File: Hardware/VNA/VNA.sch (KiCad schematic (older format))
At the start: 12 parts, among them J1 USB_B_Micro, J2 USB_A, J3 SMA, J4 SMA

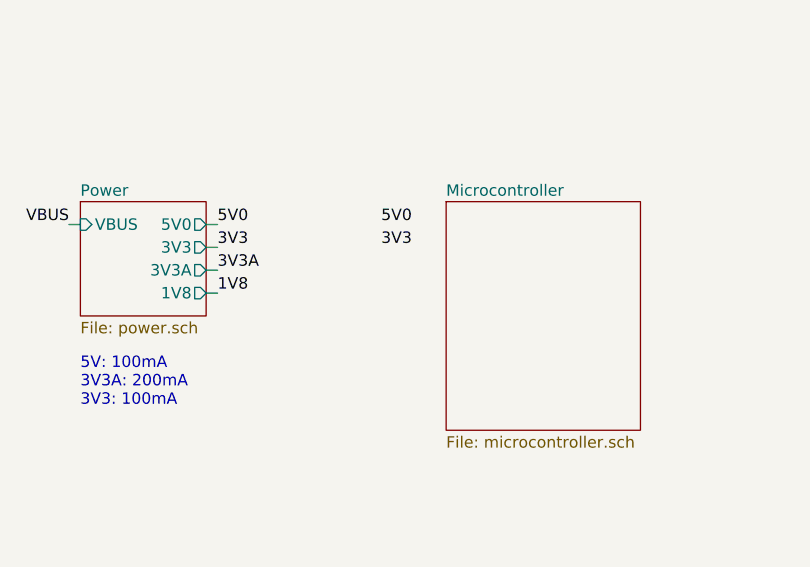
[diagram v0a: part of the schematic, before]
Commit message: added footprints and 3d models
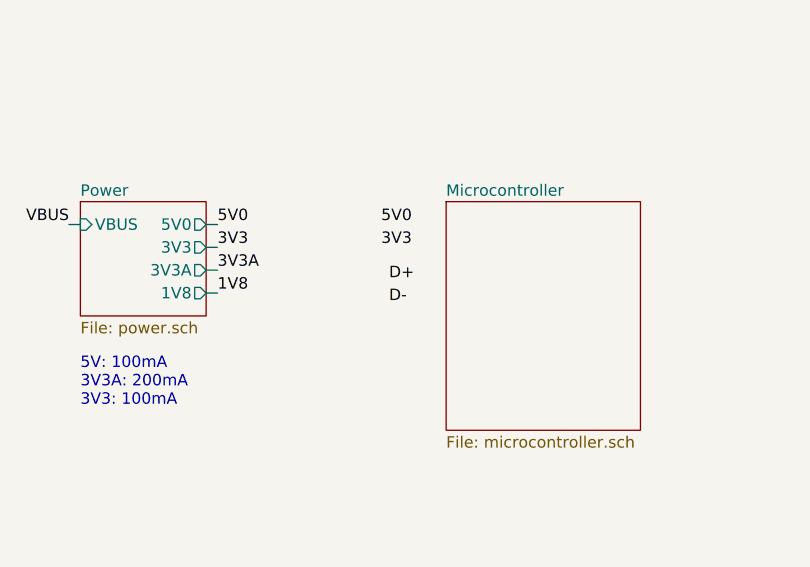
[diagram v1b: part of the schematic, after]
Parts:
- C1, C2, C3, C4: footprint (none) -> Capacitor_SMD:C_0402_1005Metric
- J1: footprint (none) -> VNA_Footprints:MicroUSB_Aliexpress
- J2: footprint (none) -> VNA_Footprints:676432911_usbA
- J3, J4: footprint (none) -> VNA_Footprints:SMA_EDGE_MOUNT
- R1, R2, R3, R4: footprint (none) -> Resistor_SMD:R_0402_1005Metric
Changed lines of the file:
@@
 F 0 "C3" V 5450 1550 50  0000 C CNN
 F 1 "1n" V 5750 1550 50  0000 C CNN
-F 2 "" H 5638 1400 50  0001 C CNN
+F 2 "Capacitor_SMD:C_0402_1005Metric" H 5638 1400 50  0001 C CNN
 F 3 "~" H 5600 1550 50  0001 C CNN
 	1    5600 1550
@@
 F 0 "C2" V 3250 1550 50  0000 C CNN
 F 1 "1n" V 3550 1550 50  0000 C CNN
-F 2 "" H 3438 1400 50  0001 C CNN
+F 2 "Capacitor_SMD:C_0402_1005Metric" H 3438 1400 50  0001 C CNN
 F 3 "~" H 3400 1550 50  0001 C CNN
 	1    3400 1550
@@
 F 0 "C1" V 2800 1800 50  0000 C CNN
 F 1 "1n" V 3100 1800 50  0000 C CNN
-F 2 "" H 2988 1650 50  0001 C CNN
+F 2 "Capacitor_SMD:C_0402_1005Metric" H 2988 1650 50  0001 C CNN
 F 3 "~" H 2950 1800 50  0001 C CNN
 	1    2950 1800
@@
 F 0 "R1" H 3370 2096 50  0000 L CNN
 F 1 "49R9" H 3370 2005 50  0000 L CNN
-F 2 "" V 3230 2050 50  0001 C CNN
+F 2 "Resistor_SMD:R_0402_1005Metric" V 3230 2050 50  0001 C CNN
 F 3 "~" H 3300 2050 50  0001 C CNN
 	1    3300 2050
@@
 F 0 "C4" V 7350 1550 50  0000 C CNN
 F 1 "1n" V 7650 1550 50  0000 C CNN
-F 2 "" H 7538 1400 50  0001 C CNN
+F 2 "Capacitor_SMD:C_0402_1005Metric" H 7538 1400 50  0001 C CNN
 F 3 "~" H 7500 1550 50  0001 C CNN
 	1    7500 1550
@@
 F 0 "J1" H 800 7450 50  0000 C CNN
 F 1 "USB_B_Micro" H 900 7350 50  0000 C CNN
-F 2 "" H 1100 6950 50  0001 C CNN
+F 2 "VNA_Footprints:MicroUSB_Aliexpress" H 1100 6950 50  0001 C CNN
 F 3 "~" H 1100 6950 50  0001 C CNN
 	1    950  7000
@@
 F 0 "J4" H 10100 1525 50  0000 L CNN
 F 1 "SMA" H 9850 1700 50  0000 L CNN
-F 2 "" H 10000 1550 50  0001 C CNN
+F 2 "VNA_Footprints:SMA_EDGE_MOUNT" H 10000 1550 50  0001 C CNN
 F 3 " ~" H 10000 1550 50  0001 C CNN
 	1    10000 1550
@@
 F 0 "R3" H 9370 2296 50  0000 L CNN
 F 1 "16R6" H 9370 2205 50  0000 L CNN
-F 2 "" V 9230 2250 50  0001 C CNN
+F 2 "Resistor_SMD:R_0402_1005Metric" V 9230 2250 50  0001 C CNN
 F 3 "~" H 9300 2250 50  0001 C CNN
 	1    9300 2250
@@
 F 0 "R2" V 9000 2500 50  0000 C CNN
 F 1 "16R6" V 9200 2500 50  0000 C CNN
-F 2 "" V 9030 2500 50  0001 C CNN
+F 2 "Resistor_SMD:R_0402_1005Metric" V 9030 2500 50  0001 C CNN
 F 3 "~" H 9100 2500 50  0001 C CNN
 	1    9100 2500
@@
 F 0 "R4" V 9400 2500 50  0000 C CNN
 F 1 "16R6" V 9600 2500 50  0000 C CNN
-F 2 "" V 9430 2500 50  0001 C CNN
+F 2 "Resistor_SMD:R_0402_1005Metric" V 9430 2500 50  0001 C CNN
 F 3 "~" H 9500 2500 50  0001 C CNN
 	1    9500 2500
@@
 F 0 "J3" H 10050 4475 50  0000 L CNN
 F 1 "SMA" H 9800 4650 50  0000 L CNN
-F 2 "" H 9950 4500 50  0001 C CNN
+F 2 "VNA_Footprints:SMA_EDGE_MOUNT" H 9950 4500 50  0001 C CNN
 F 3 " ~" H 9950 4500 50  0001 C CNN
 	1    9950 4500
@@
 F 0 "J2" H 1850 7450 50  0000 C CNN
 F 1 "USB_A" H 1900 7350 50  0000 C CNN
-F 2 "" H 2150 6950 50  0001 C CNN
+F 2 "VNA_Footprints:676432911_usbA" H 2150 6950 50  0001 C CNN
 F 3 " ~" H 2150 6950 50  0001 C CNN
 	1    2000 7000
@@
 Text Label 6150 2350 2    50   ~ 0
 PA_PWRDN
+Text Label 3000 4550 0    50   ~ 0
+D+
+Text Label 3000 4650 0    50   ~ 0
+D-
 $EndSCHEMATC

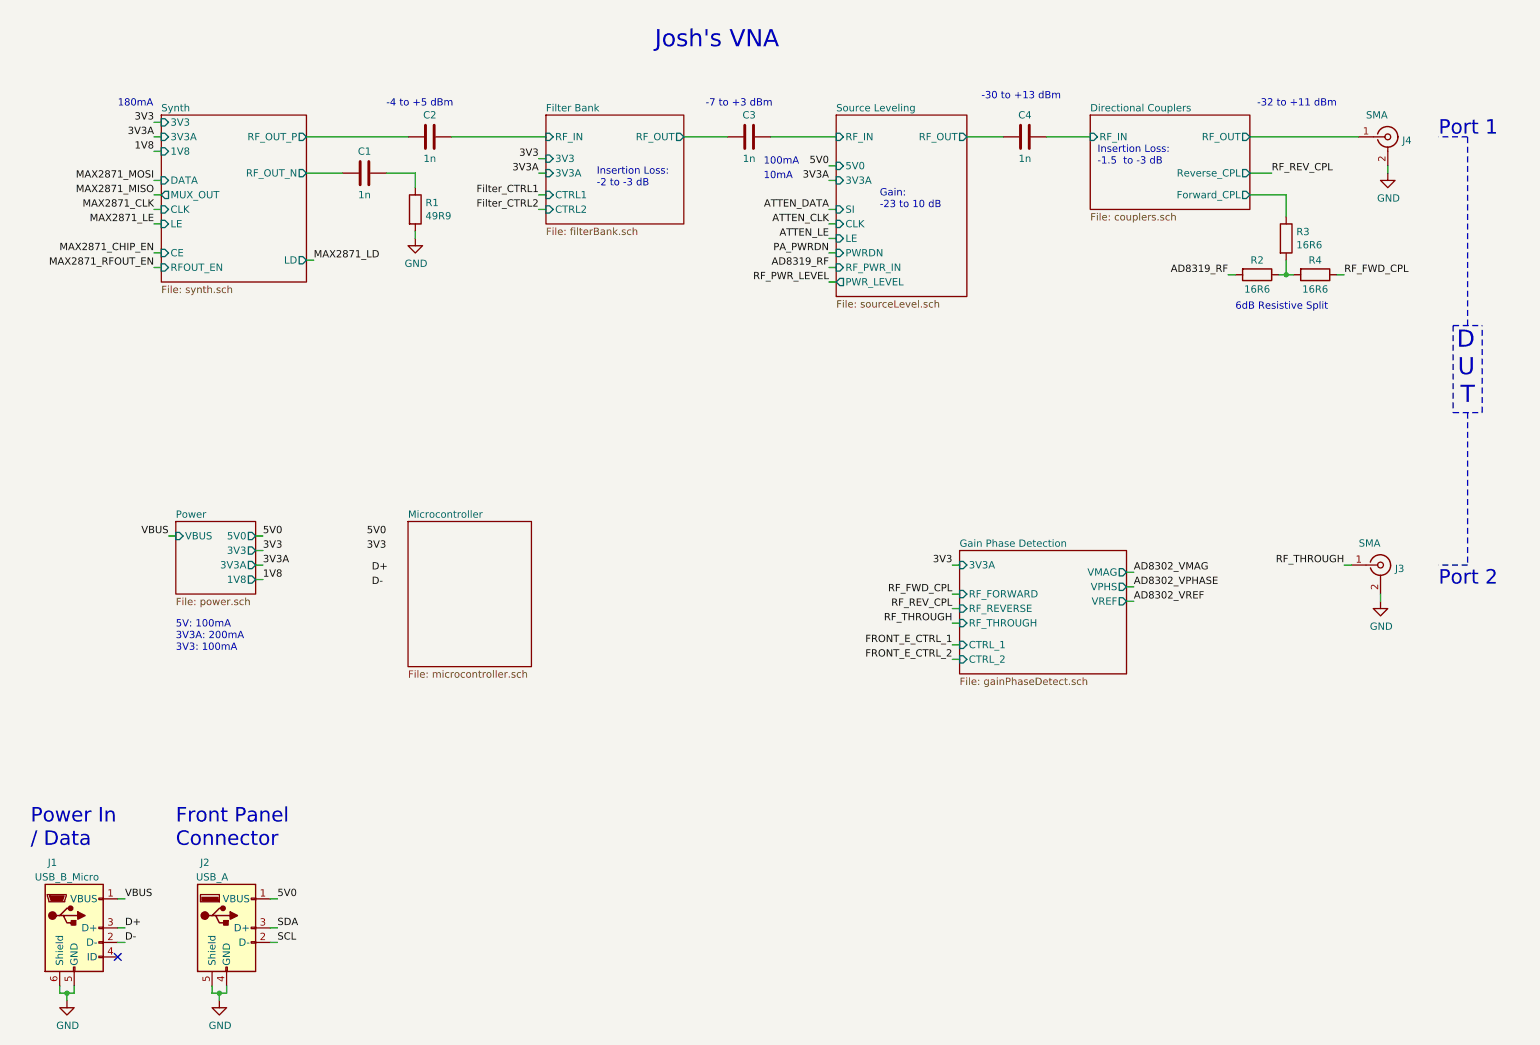
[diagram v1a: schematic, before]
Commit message: prelim schematic capture complete
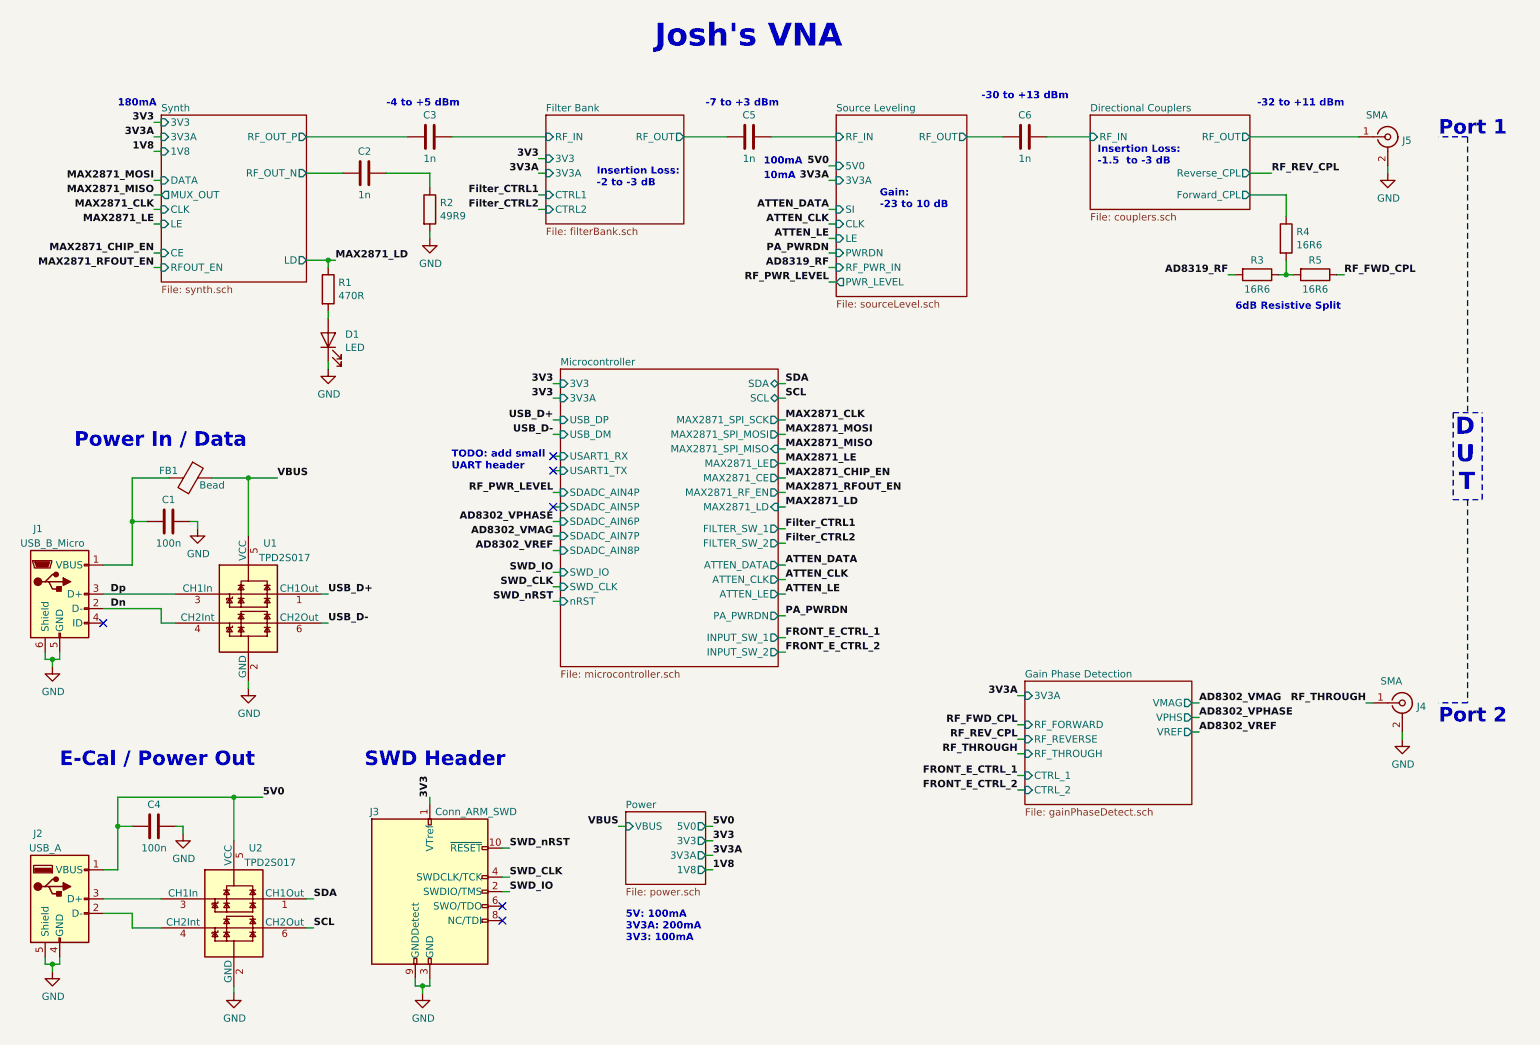
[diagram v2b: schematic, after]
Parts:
- added C1, C4: 100n, symbol Device:C
- added D1: LED, symbol Device:LED
- added FB1: Bead, symbol VNA_Symbols:Ferrite_Bead_PWR
- added J3: Conn_ARM_SWD, symbol Connector:Conn_ARM_JTAG_SWD_10
- added R1: 470R, symbol Device:R
- added U1, U2: TPD2S017, Package_TO_SOT_SMD:SOT-23-6, symbol Power_Protection:TPD2S017
- renumbered C1 to C2, C2 to C3, C3 to C5, C4 to C6, J3 to J4, J4 to J5, R1 to R2, R2 to R3, R3 to R4, R4 to R5
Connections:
- net 3V3: now also J3.1 (VTref)
- net 5V0: now also C4.1, U2.5 (VCC)
- net GND: now also C1.2, C4.2, D1.1 (K), J3.3 (GND), J3.5 (GND), J3.9 (GNDDetect), U1.2 (GND), U2.2 (GND)
- net MAX2871_LD: now also R1.1
- net SCL: now also U2.6 (CH2Out); no longer J2.2 (D-)
- net SDA: now also U2.1 (CH1Out); no longer J2.3 (D+)
- net VBUS: now also FB1.1, U1.5 (VCC); no longer J1.1 (VBUS)
- net D+ renamed Dp
- net Dp: now also U1.3 (CH1In)
- net D- renamed Dn
- net Dn: now also U1.4 (CH2Int)
- new net: C1.1, FB1.2, J1.1 (VBUS)
- new net: J2.3 (D+), U2.3 (CH1In)
- new net: J2.2 (D-), U2.4 (CH2Int)
- new net: D1.2 (A), R1.2
- new net SWD_CLK: J3.4 (SWDCLK/TCK)
- new net SWD_IO: J3.2 (SWDIO/TMS)
- new net SWD_nRST: J3.10 (~RESET~)
- new net USB_D+: U1.1 (CH1Out)
- new net USB_D-: U1.6 (CH2Out)
- no-connect marks 1 -> 6
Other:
- note added: "E-Cal / Power Out"
- note added: "Power In / Data"
- note added: "SWD Header"
- note added: "TODO: add small \nUART header"
- note removed: "Front Panel \nConnector"
- note removed: "Power In \n/ Data"
- moved on the sheet: J1, J2, J4, R2

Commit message: all 3d models created, prelim bom generated
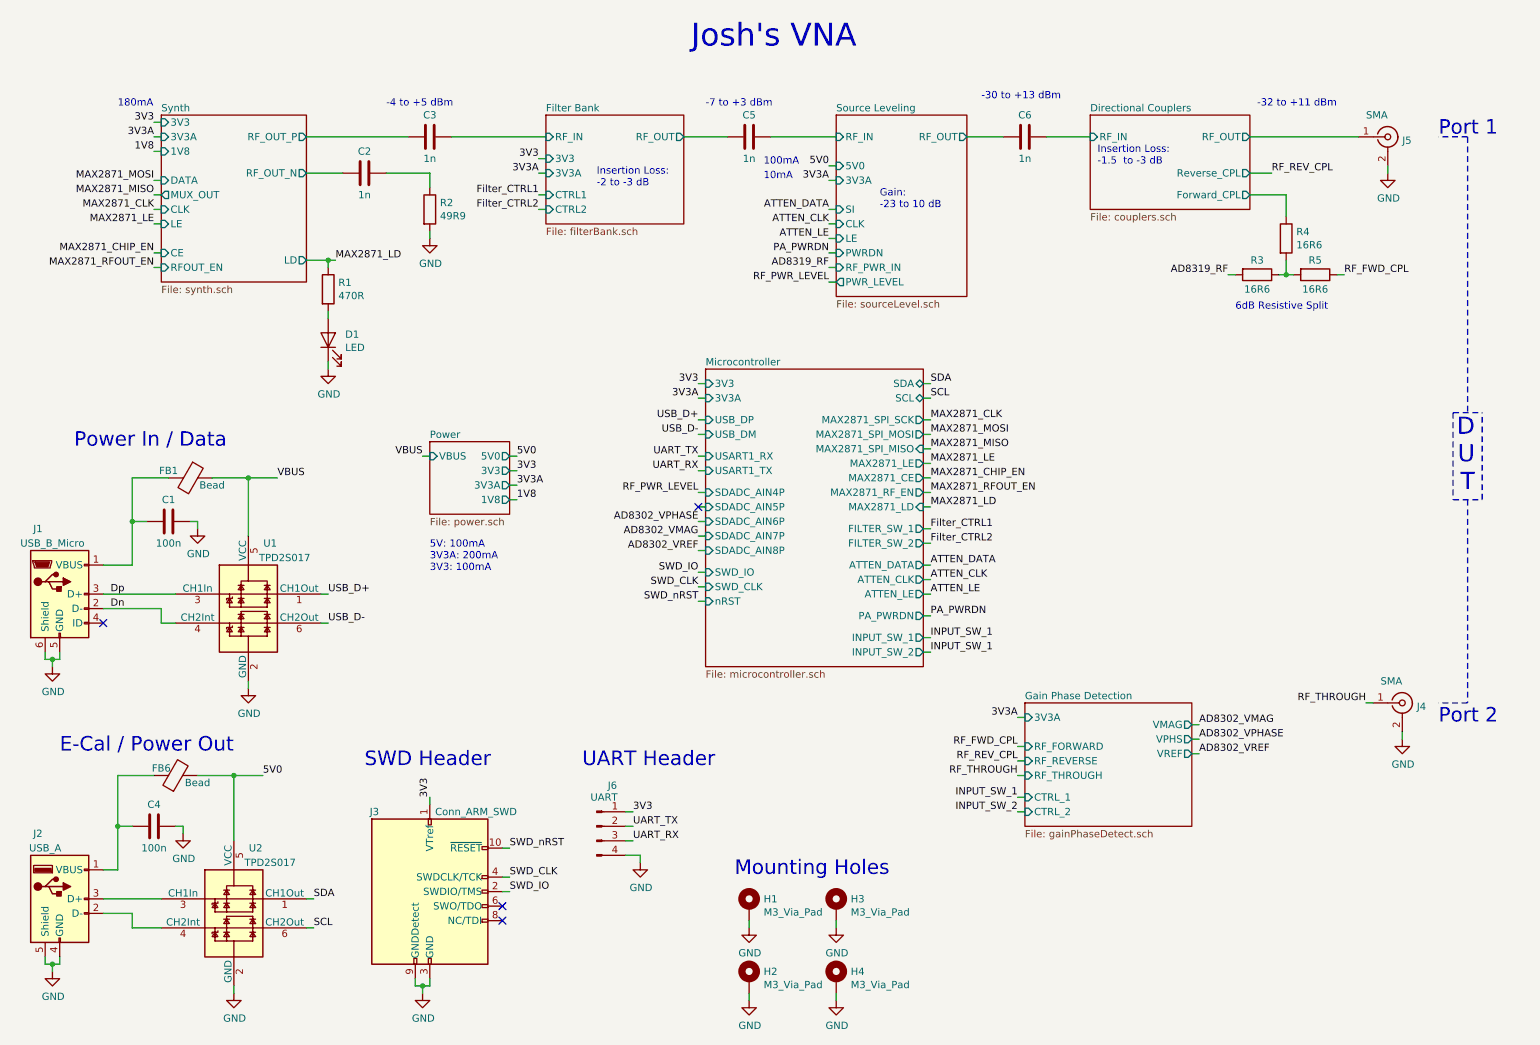
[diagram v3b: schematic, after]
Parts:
- added FB6: Bead, VNA_Footprints:BEADC1608X95N, symbol VNA_Symbols:Ferrite_Bead_PWR
- added H1, H2, H3, H4: M3_Via_Pad, MountingHole:MountingHole_3.2mm_M3_Pad_Via, symbol Mechanical:MountingHole_Pad
- added J6: UART, Connector_JST:JST_GH_BM04B-GHS-TBT_1x04-1MP_P1.25mm_Vertical, symbol Connector:Conn_01x04_Male
- C1, C4: footprint (none) -> Capacitor_SMD:C_0603_1608Metric
- D1: footprint (none) -> LED_SMD:LED_0603_1608Metric
- FB1: footprint (none) -> VNA_Footprints:BEADC1608X95N
- J3: footprint (none) -> VNA_Footprints:SAMTEC_FTSH-105-01-L-DV-R-TR
- R1: footprint (none) -> Resistor_SMD:R_0603_1608Metric
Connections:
- net 3V3: now also J6.1 (Pin_1)
- net 5V0: now also FB6.2; no longer C4.1, J2.1 (VBUS)
- net GND: now also H1.1, H2.1, H3.1, H4.1, J6.4 (Pin_4)
- new net: C4.1, FB6.1, J2.1 (VBUS)
- new net UART_RX: J6.3 (Pin_3)
- new net UART_TX: J6.2 (Pin_2)
- no-connect marks 6 -> 4
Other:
- note added: "Mounting Holes"
- note added: "UART Header"
- note removed: "TODO: add small \nUART header"

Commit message: More schematic changes + updated functionals
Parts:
- added R61: 0R0, Resistor_SMD:R_0603_1608Metric, symbol Device:R
- added TP43: 5V_VIN, VNA_Footprints:TestPoint_Loop_D1.80mm_Drill1.0mm_Beaded_RED, symbol Connector:TestPoint
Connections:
- net at C1.1, FB1.2: now also R61.1, TP43.1; no longer J1.1 (VBUS)
- new net: J1.1 (VBUS), R61.2
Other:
- moved on the sheet: C1, FB1, U1

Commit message: first day of layout / routing done
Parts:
- J4, J5: footprint VNA_Footprints:SMA_EDGE_MOUNT -> VNA_Footprints:SMA_EDGE_MOUNT_INSET
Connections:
- net Dn: now also U1.3 (CH1In); no longer U1.4 (CH2Int)
- net Dp: now also U1.4 (CH2Int); no longer U1.3 (CH1In)
- net USB_D+: now also U1.6 (CH2Out); no longer U1.1 (CH1Out)
- net USB_D-: now also U1.1 (CH1Out); no longer U1.6 (CH2Out)

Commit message: more routing progress
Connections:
- net UART_RX: now also J6.2 (Pin_2); no longer J6.3 (Pin_3)
- net UART_TX: now also J6.3 (Pin_3); no longer J6.2 (Pin_2)
- net Dn renamed D_N
- net Dp renamed D_P
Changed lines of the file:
@@
 $EndComp
 Text Label 1200 4700 0    50   ~ 10
-Dp
+D_P
 Text Label 1200 4800 0    50   ~ 10
-Dn
+D_N
 Text Notes 950  3700 0    100  ~ 20
 Power In / Data
@@
 Text Label 6850 4800 0    50   ~ 10
 ATTEN_LE
-Text Label 5250 4000 2    50   ~ 10
+Text Label 5250 4100 2    50   ~ 10
 RF_PWR_LEVEL
 Text Label 6850 4950 0    50   ~ 10
@@
 Text Label 5250 4400 2    50   ~ 10
 AD8302_VREF
-Text Label 5250 4200 2    50   ~ 10
+Text Label 5250 4300 2    50   ~ 10
 AD8302_VPHASE
-Text Label 5250 4300 2    50   ~ 10
-AD8302_VMAG
-NoConn ~ 5250 4100
 $Comp
 L VNA_Symbols:Ferrite_Bead_PWR FB1
@@
 Text Label 5250 3850 2    50   ~ 10
 UART_RX
+Text Label 4800 6400 0    50   ~ 10
+UART_TX
 Text Label 4800 6300 0    50   ~ 10
-UART_TX
-Text Label 4800 6400 0    50   ~ 10
 UART_RX
 Wire Wire Line
@@
 Wire Wire Line
 	1150 4700 1400 4700
+Text Label 5250 4000 2    50   ~ 10
+AD8302_VMAG
+NoConn ~ 5250 4200
 $EndSCHEMATC

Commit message: no unrouted nets!
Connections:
- net at U2.3 (CH1In): now also J2.2 (D-); no longer J2.3 (D+)
- net at U2.4 (CH2Int): now also J2.3 (D+); no longer J2.2 (D-)
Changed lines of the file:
@@
 5V0
 Wire Wire Line
-	1150 6800 1550 6800
-Wire Wire Line
-	1350 6900 1350 7000
-Wire Wire Line
 	1350 7000 1550 7000
 Wire Wire Line
-	1150 6900 1350 6900
+	1150 6800 1350 6800
 Wire Wire Line
 	2250 3900 2500 3900
@@
 INPUT_SW_1
 Text Label 6850 5200 0    50   ~ 10
-INPUT_SW_1
+INPUT_SW_2
 $Comp
 L Connector:Conn_01x04_Male J6
@@
 AD8302_VMAG
 NoConn ~ 5250 4200
+Wire Wire Line
+	1350 6800 1350 7000
+Wire Wire Line
+	1550 6800 1450 6800
+Wire Wire Line
+	1450 6800 1450 6900
+Wire Wire Line
+	1450 6900 1150 6900
 $EndSCHEMATC
